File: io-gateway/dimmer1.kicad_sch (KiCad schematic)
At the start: 1 part, among them U1 LED5000

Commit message: update
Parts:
- added C22, C29, C33, C35: 100nF 50V, Capacitor_SMD:C_0201_0603Metric, symbol Device:C
- added C23, C36: 1µF 50V, Capacitor_SMD:C_1206_3216Metric, symbol Device:C
- added C24, C37: NM, Capacitor_SMD:C_1206_3216Metric, symbol Device:C
- added C25, C34: 22pF, Capacitor_SMD:C_0603_1608Metric, symbol Device:C
- added C26, C32: 470pF, Capacitor_SMD:C_0603_1608Metric, symbol Device:C
- added C27, C28, C30, C31: 10µF 50V, Capacitor_SMD:C_1210_3225Metric, symbol Device:C
- added D20, D23: D_Zener, Diode_SMD:D_SOD-123, symbol Device:D_Zener
- added D21, D22: D_Schottky, Diode_SMD:D_SMB, symbol Device:D_Schottky
- added L4, L5: 47µH 3.8A, Inductor_SMD:L_12x12mm_H8mm, symbol Device:L
- added R38, R41: 47k, Resistor_SMD:R_0603_1608Metric, symbol Device:R
- added R39, R40: 24k9, Resistor_SMD:R_0603_1608Metric, symbol Device:R
- added RS_DIM1, RS_DIM2: R, Resistor_SMD:R_1206_3216Metric, symbol Device:R
- added U2: LED5000, Package_SO:HSOP-8-1EP_3.9x4.9mm_P1.27mm_EP2.41x3.1mm, symbol Driver_LED:LED5000
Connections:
- net at U1.1 (BOOT): now also C22.1
- net PWM_DIM1: now reaches U1.2 (DIM)
- net INH_DIM1: now reaches U1.3 (INH)
- net at U1.4 (COMP): now also C25.1, R39.2
- net at U1.5 (FB): now also D20.2 (A), R38.2
- net GND: now reaches U1.6 (GND), U1.9 (GND)
- net GND: now also U1.7 (VIN), C23.2, C25.2, C26.2, C27.1, C27.2, C28.1, C28.2, C29.1, C29.2, C30.1, C30.2, C31.1, C31.2, C32.2, C33.1, C33.2, C34.2, C36.2, D21.2 (A), D22.2 (A), RS_DIM1.2, RS_DIM2.2, U2.6 (GND), U2.7 (VIN), U2.9 (GND)
- net at U1.8 (SW): now also C22.2, D21.1 (K), L4.2
- new net: C26.1, R39.1
- new net: C35.1, U2.1 (BOOT)
- new net: C34.1, R40.2, U2.4 (COMP)
- new net: D23.2 (A), R41.2, U2.5 (FB)
- new net: C35.2, D22.1 (K), L5.2, U2.8 (SW)
- new net: C32.1, R40.1
- new net DIM1_VLED+: C23.1, C24.1, D20.1 (K), L4.1
- new net DIM1_VLED-: C24.2, R38.1, RS_DIM1.1
- new net DIM2_VLED+: C36.1, C37.1, D23.1 (K), L5.1
- new net DIM2_VLED-: C37.2, R41.1, RS_DIM2.1
- new net INH_DIM2: U2.3 (INH)
- new net PWM_DIM2: U2.2 (DIM)
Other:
- moved on the sheet: U1

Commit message: layout for first dimmer
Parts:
- C22: footprint Capacitor_SMD:C_0201_0603Metric -> Capacitor_SMD:C_0603_1608Metric
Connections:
- net GND: no longer C27.1, C28.1, C29.1, C30.1, C31.1, C33.1, U1.7 (VIN), U2.7 (VIN)
- net DIM1_FB: now reaches D20.2 (A), R38.2, U1.5 (FB)
- net DIM1_SW: now reaches C22.2, D21.1 (K), L4.2, U1.8 (SW)
- net DIM1_VLED+ renamed DIM1_VLED_VCC
- net DIM1_VLED- renamed DIM1_VLED_GND
- net DIM2_VLED+ renamed DIM2_VLED_VCC
- net DIM2_VLED- renamed DIM2_VLED_GND
- new net VIN_DIM1: C27.1, C28.1, C29.1, C30.1, C31.1, C33.1, U1.7 (VIN), U2.7 (VIN)
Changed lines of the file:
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@@
 		)
 	)
-	(global_label "DIM1_VLED-"
-		(shape input)
-		(at 201.93 60.96 0)
-		(fields_autoplaced yes)
+	(label "DIM1_SW"
+		(at 114.3 46.99 0)
 		(effects
 			(font
 				(size 1.27 1.27)
 			)
+			(justify left bottom)
+		)
+	)
+	(label "DIM1_FB"
+		(at 114.3 49.53 0)
+		(effects
+			(font
+				(size 1.27 1.27)
+			)
+			(justify left bottom)
+		)
+	)
+	(global_label "DIM1_VLED_GND"
+		(shape input)
+		(at 201.93 60.96 0)
+		(fields_autoplaced yes)
+		(effects
+			(font
+				(size 1.27 1.27)
+			)
 			(justify left)
 		)
@@
 		)
 	)
-	(global_label "DIM1_VLED+"
+	(global_label "DIM1_VLED_VCC"
 		(shape input)
 		(at 201.93 46.99 0)
@@
 		)
 	)
-	(global_label "DIM2_VLED-"
+	(global_label "DIM2_VLED_GND"
 		(shape input)
 		(at 200.66 135.89 0)
@@
 		)
 	)
-	(global_label "VIN_DIM1"
+	(global_label "GND_DIM1"
 		(shape input)
 		(at 33.02 78.74 180)
@@
 		)
 		(property "Intersheetrefs" "${INTERSHEET_REFS}"
-			(at 21.5076 78.74 0)
+			(at 20.661 78.74 0)
 			(effects
 				(font
@@
 		)
 	)
-	(global_label "DIM2_VLED+"
+	(global_label "DIM2_VLED_VCC"
 		(shape input)
 		(at 200.66 121.92 0)
@@
 			)
 		)
-		(property "Footprint" "Capacitor_SMD:C_0201_0603Metric"
+		(property "Footprint" "Capacitor_SMD:C_0603_1608Metric"
 			(at 133.0452 46.99 0)
 			(effects

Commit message: upd
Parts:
- C29, C33, C35: footprint Capacitor_SMD:C_0201_0603Metric -> Capacitor_SMD:C_0603_1608Metric
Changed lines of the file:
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@@
 	)
 	(junction
+		(at 71.12 78.74)
+		(diameter 0)
+		(color 0 0 0 0)
+	)
+	(junction
 		(at 130.81 154.94)
 		(diameter 0)
@@
 	)
 	(junction
+		(at 38.1 78.74)
+		(diameter 0)
+		(color 0 0 0 0)
+	)
+	(junction
 		(at 96.52 154.94)
 		(diameter 0)
@@
 	(wire
 		(pts
+			(xy 71.12 78.74) (xy 71.12 80.01)
+		)
+		(stroke
+			(width 0)
+			(type default)
+		)
+	)
+	(wire
+		(pts
 			(xy 97.79 82.55) (xy 97.79 80.01)
 		)
@@
 	(wire
 		(pts
-			(xy 71.12 72.39) (xy 71.12 80.01)
+			(xy 71.12 72.39) (xy 71.12 78.74)
 		)
 		(stroke
@@
 	(wire
 		(pts
+			(xy 38.1 78.74) (xy 71.12 78.74)
+		)
+		(stroke
+			(width 0)
+			(type default)
+		)
+	)
+	(wire
+		(pts
 			(xy 31.75 121.92) (xy 86.36 121.92)
 		)
@@
 			)
 		)
-		(property "Footprint" "Capacitor_SMD:C_0201_0603Metric"
+		(property "Footprint" "Capacitor_SMD:C_0603_1608Metric"
 			(at 77.1652 107.95 0)
 			(effects
@@
 			)
 		)
-		(property "Footprint" "Capacitor_SMD:C_0201_0603Metric"
+		(property "Footprint" "Capacitor_SMD:C_0603_1608Metric"
 			(at 78.4352 33.02 0)
 			(effects
@@
 			)
 		)
-		(property "Footprint" "Capacitor_SMD:C_0201_0603Metric"
+		(property "Footprint" "Capacitor_SMD:C_0603_1608Metric"
 			(at 131.7752 121.92 0)
 			(effects

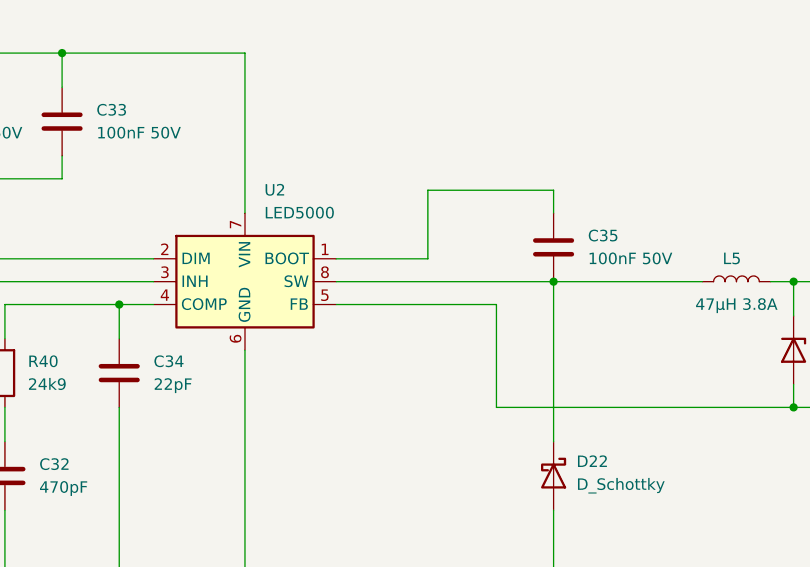
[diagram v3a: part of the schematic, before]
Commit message: add second dimmer
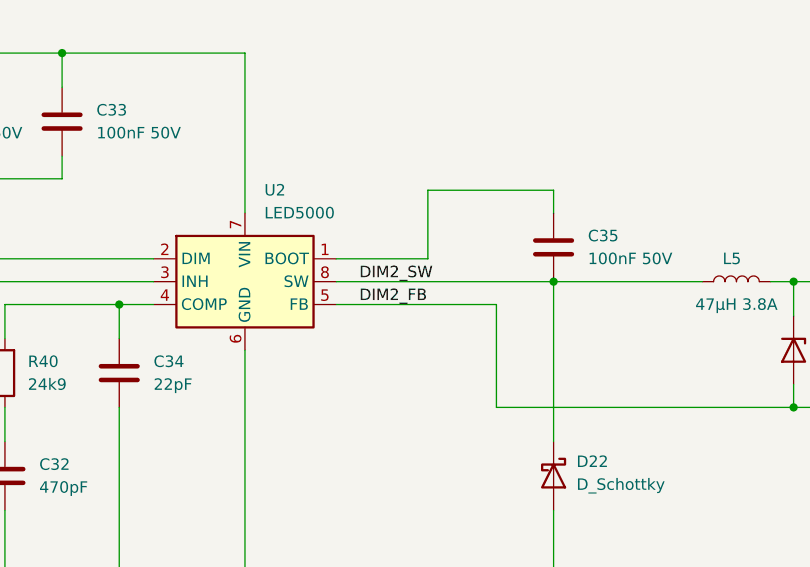
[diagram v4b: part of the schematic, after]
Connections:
- net DIM2_FB: now reaches D23.2 (A), R41.2, U2.5 (FB)
- net DIM2_SW: now reaches C35.2, D22.1 (K), L5.2, U2.8 (SW)
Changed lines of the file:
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@@
+		)
+	)
+	(label "DIM2_SW"
+		(at 109.22 121.92 0)
+		(effects
+			(font
+				(size 1.27 1.27)
+			)
+			(justify left bottom)
+		)
+	)
+	(label "DIM2_FB"
+		(at 109.22 124.46 0)
+		(effects
+			(font
+				(size 1.27 1.27)
+			)
+			(justify left bottom)
 		)
 	)

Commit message: temp
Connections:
- net DIM1_VLED_GND renamed DIM_VLED-_A
- net DIM1_VLED_VCC renamed DIM_VLED+_A
- net DIM2_VLED_GND renamed DIM_VLED-_B
- net DIM2_VLED_VCC renamed DIM_VLED+_B
- net INH_DIM1 renamed INH_DIMA
- net INH_DIM2 renamed INH_DIMB
- net PWM_DIM1 renamed PWM_DIMA
- net PWM_DIM2 renamed PWM_DIMB
- net VIN_DIM1 renamed VIN_DIM
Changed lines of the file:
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@@
 	(wire
 		(pts
-			(xy 31.75 119.38) (xy 86.36 119.38)
+			(xy 26.67 119.38) (xy 86.36 119.38)
 		)
 		(stroke
@@
 	(wire
 		(pts
-			(xy 195.58 46.99) (xy 201.93 46.99)
+			(xy 195.58 46.99) (xy 223.52 46.99)
 		)
 		(stroke
@@
 	(wire
 		(pts
-			(xy 195.58 60.96) (xy 201.93 60.96)
+			(xy 195.58 60.96) (xy 223.52 60.96)
 		)
 		(stroke
@@
 	(wire
 		(pts
-			(xy 194.31 135.89) (xy 200.66 135.89)
+			(xy 194.31 135.89) (xy 220.98 135.89)
 		)
 		(stroke
@@
 	(wire
 		(pts
-			(xy 33.02 46.99) (xy 87.63 46.99)
-		)
-		(stroke
-			(width 0)
-			(type default)
-		)
-	)
-	(wire
-		(pts
 			(xy 83.82 60.96) (xy 83.82 80.01)
 		)
@@
 	(wire
 		(pts
+			(xy 21.59 21.59) (xy 43.18 21.59)
+		)
+		(stroke
+			(width 0)
+			(type default)
+		)
+	)
+	(wire
+		(pts
 			(xy 191.77 46.99) (xy 195.58 46.99)
 		)
@@
 	(wire
 		(pts
+			(xy 24.13 44.45) (xy 87.63 44.45)
+		)
+		(stroke
+			(width 0)
+			(type default)
+		)
+	)
+	(wire
+		(pts
 			(xy 96.52 157.48) (xy 96.52 154.94)
 		)
@@
 	(wire
 		(pts
-			(xy 33.02 44.45) (xy 87.63 44.45)
-		)
-		(stroke
-			(width 0)
-			(type default)
-		)
-	)
-	(wire
-		(pts
 			(xy 177.8 80.01) (xy 191.77 80.01)
 		)
@@
 	(wire
 		(pts
-			(xy 43.18 21.59) (xy 31.75 21.59)
-		)
-		(stroke
-			(width 0)
-			(type default)
-		)
-	)
-	(wire
-		(pts
 			(xy 132.08 36.83) (xy 132.08 39.37)
 		)
@@
 	(wire
 		(pts
-			(xy 194.31 121.92) (xy 200.66 121.92)
+			(xy 194.31 121.92) (xy 220.98 121.92)
 		)
 		(stroke
@@
 	(wire
 		(pts
+			(xy 24.13 46.99) (xy 87.63 46.99)
+		)
+		(stroke
+			(width 0)
+			(type default)
+		)
+	)
+	(wire
+		(pts
 			(xy 41.91 107.95) (xy 41.91 110.49)
 		)
@@
 	(wire
 		(pts
-			(xy 33.02 78.74) (xy 38.1 78.74)
-		)
-		(stroke
-			(width 0)
-			(type default)
-		)
-	)
-	(wire
-		(pts
 			(xy 96.52 114.3) (xy 96.52 96.52)
 		)
@@
 	(wire
 		(pts
-			(xy 31.75 121.92) (xy 86.36 121.92)
+			(xy 26.67 121.92) (xy 86.36 121.92)
 		)
 		(stroke
@@
 		(pts
 			(xy 96.52 154.94) (xy 130.81 154.94)
+		)
+		(stroke
+			(width 0)
+			(type default)
+		)
+	)
+	(wire
+		(pts
+			(xy 22.86 78.74) (xy 38.1 78.74)
 		)
 		(stroke
@@
 		)
 	)
+	(label "VIN_DIM"
+		(at 30.48 96.52 0)
+		(effects
+			(font
+				(size 1.27 1.27)
+			)
+			(justify left bottom)
+		)
+	)
 	(label "DIM2_SW"
 		(at 109.22 121.92 0)
@@
 		)
 	)
-	(global_label "DIM1_VLED_GND"
+	(hierarchical_label "INH_DIMB"
 		(shape input)
-		(at 201.93 60.96 0)
-		(fields_autoplaced yes)
+		(at 26.67 121.92 180)
+		(effects
+			(font
+				(size 1.27 1.27)
+			)
+			(justify right)
+		)
+	)
+	(hierarchical_label "DIM_VLED+_A"
+		(shape output)
+		(at 223.52 46.99 0)
 		(effects
 			(font
@@
 			(justify left)
 		)
-		(property "Intersheetrefs" "${INTERSHEET_REFS}"
-			(at 216.5266 60.96 0)
-			(effects
-				(font
-					(size 1.27 1.27)
-				)
-				(justify left)
-				(hide yes)
-			)
-		)
-	)
-	(global_label "VIN_DIM1"
+	)
+	(hierarchical_label "DIM_VLED-_A"
+		(shape output)
+		(at 223.52 60.96 0)
+		(effects
+			(font
+				(size 1.27 1.27)
+			)
+			(justify left)
+		)
+	)
+	(hierarchical_label "VIN_DIM"
 		(shape input)
-		(at 31.75 21.59 180)
-		(fields_autoplaced yes)
+		(at 21.59 21.59 180)
 		(effects
 			(font
@@
 			(justify right)
 		)
-		(property "Intersheetrefs" "${INTERSHEET_REFS}"
-			(at 20.2376 21.59 0)
-			(effects
-				(font
-					(size 1.27 1.27)
-				)
-				(justify right)
-				(hide yes)
-			)
-		)
-	)
-	(global_label "DIM1_VLED_VCC"
+	)
+	(hierarchical_label "INH_DIMA"
 		(shape input)
-		(at 201.93 46.99 0)
-		(fields_autoplaced yes)
+		(at 24.13 46.99 180)
+		(effects
+			(font
+				(size 1.27 1.27)
+			)
+			(justify right)
+		)
+	)
+	(hierarchical_label "PWM_DIMB"
+		(shape input)
+		(at 26.67 119.38 180)
+		(effects
+			(font
+				(size 1.27 1.27)
+			)
+			(justify right)
+		)
+	)
+	(hierarchical_label "DIM_VLED+_B"
+		(shape output)
+		(at 220.98 121.92 0)
 		(effects
 			(font
@@
 			(justify left)
 		)
-		(property "Intersheetrefs" "${INTERSHEET_REFS}"
-			(at 216.5266 46.99 0)
-			(effects
-				(font
-					(size 1.27 1.27)
-				)
-				(justify left)
-				(hide yes)
-			)
-		)
-	)
-	(global_label "PWM_DIM1"
+	)
+	(hierarchical_label "PWM_DIMA"
 		(shape input)
-		(at 33.02 44.45 180)
-		(fields_autoplaced yes)
+		(at 24.13 44.45 180)
 		(effects
 			(font
@@
 			(justify right)
 		)
-		(property "Intersheetrefs" "${INTERSHEET_REFS}"
-			(at 20.3587 44.45 0)
-			(effects
-				(font
-					(size 1.27 1.27)
-				)
-				(justify right)
-				(hide yes)
-			)
-		)
-	)
-	(global_label "VIN_DIM1"
+	)
+	(hierarchical_label "GND_DIM"
 		(shape input)
-		(at 30.48 96.52 180)
-		(fields_autoplaced yes)
+		(at 22.86 78.74 180)
 		(effects
 			(font
@@
 			(justify right)
 		)
-		(property "Intersheetrefs" "${INTERSHEET_REFS}"
-			(at 18.9676 96.52 0)
-			(effects
-				(font
-					(size 1.27 1.27)
-				)
-				(justify right)
-				(hide yes)
-			)
-		)
-	)
-	(global_label "DIM2_VLED_GND"
-		(shape input)
-		(at 200.66 135.89 0)
-		(fields_autoplaced yes)
+	)
+	(hierarchical_label "DIM_VLED-_B"
+		(shape output)
+		(at 220.98 135.89 0)
 		(effects
 			(font
@@
 			(justify left)
 		)
-		(property "Intersheetrefs" "${INTERSHEET_REFS}"
-			(at 215.2566 135.89 0)
-			(effects
-				(font
-					(size 1.27 1.27)
-				)
-				(justify left)
-				(hide yes)
-			)
-		)
-	)
-	(global_label "GND_DIM1"
-		(shape input)
-		(at 33.02 78.74 180)
-		(fields_autoplaced yes)
-		(effects
-			(font
-				(size 1.27 1.27)
-			)
-			(justify right)
-		)
-		(property "Intersheetrefs" "${INTERSHEET_REFS}"
-			(at 20.661 78.74 0)
-			(effects
-				(font
-					(size 1.27 1.27)
-				)
-				(justify right)
-				(hide yes)
-			)
-		)
-	)
-	(global_label "PWM_DIM2"
-		(shape input)
-		(at 31.75 119.38 180)
-		(fields_autoplaced yes)
-		(effects
-			(font
-				(size 1.27 1.27)
-			)
-			(justify right)
-		)
-		(property "Intersheetrefs" "${INTERSHEET_REFS}"
-			(at 19.0887 119.38 0)
-			(effects
-				(font
-					(size 1.27 1.27)
-				)
-				(justify right)
-				(hide yes)
-			)
-		)
-	)
-	(global_label "INH_DIM2"
-		(shape input)
-		(at 31.75 121.92 180)
-		(fields_autoplaced yes)
-		(effects
-			(font
-				(size 1.27 1.27)
-			)
-			(justify right)
-		)
-		(property "Intersheetrefs" "${INTERSHEET_REFS}"
-			(at 19.9957 121.92 0)
-			(effects
-				(font
-					(size 1.27 1.27)
-				)
-				(justify right)
-				(hide yes)
-			)
-		)
-	)
-	(global_label "INH_DIM1"
-		(shape input)
-		(at 33.02 46.99 180)
-		(fields_autoplaced yes)
-		(effects
-			(font
-				(size 1.27 1.27)
-			)
-			(justify right)
-		)
-		(property "Intersheetrefs" "${INTERSHEET_REFS}"
-			(at 21.2657 46.99 0)
-			(effects
-				(font
-					(size 1.27 1.27)
-				)
-				(justify right)
-				(hide yes)
-			)
-		)
-	)
-	(global_label "DIM2_VLED_VCC"
-		(shape input)
-		(at 200.66 121.92 0)
-		(fields_autoplaced yes)
-		(effects
-			(font
-				(size 1.27 1.27)
-			)
-			(justify left)
-		)
-		(property "Intersheetrefs" "${INTERSHEET_REFS}"
-			(at 215.2566 121.92 0)
-			(effects
-				(font
-					(size 1.27 1.27)
-				)
-				(justify left)
-				(hide yes)
-			)
-		)
-	)
+	)

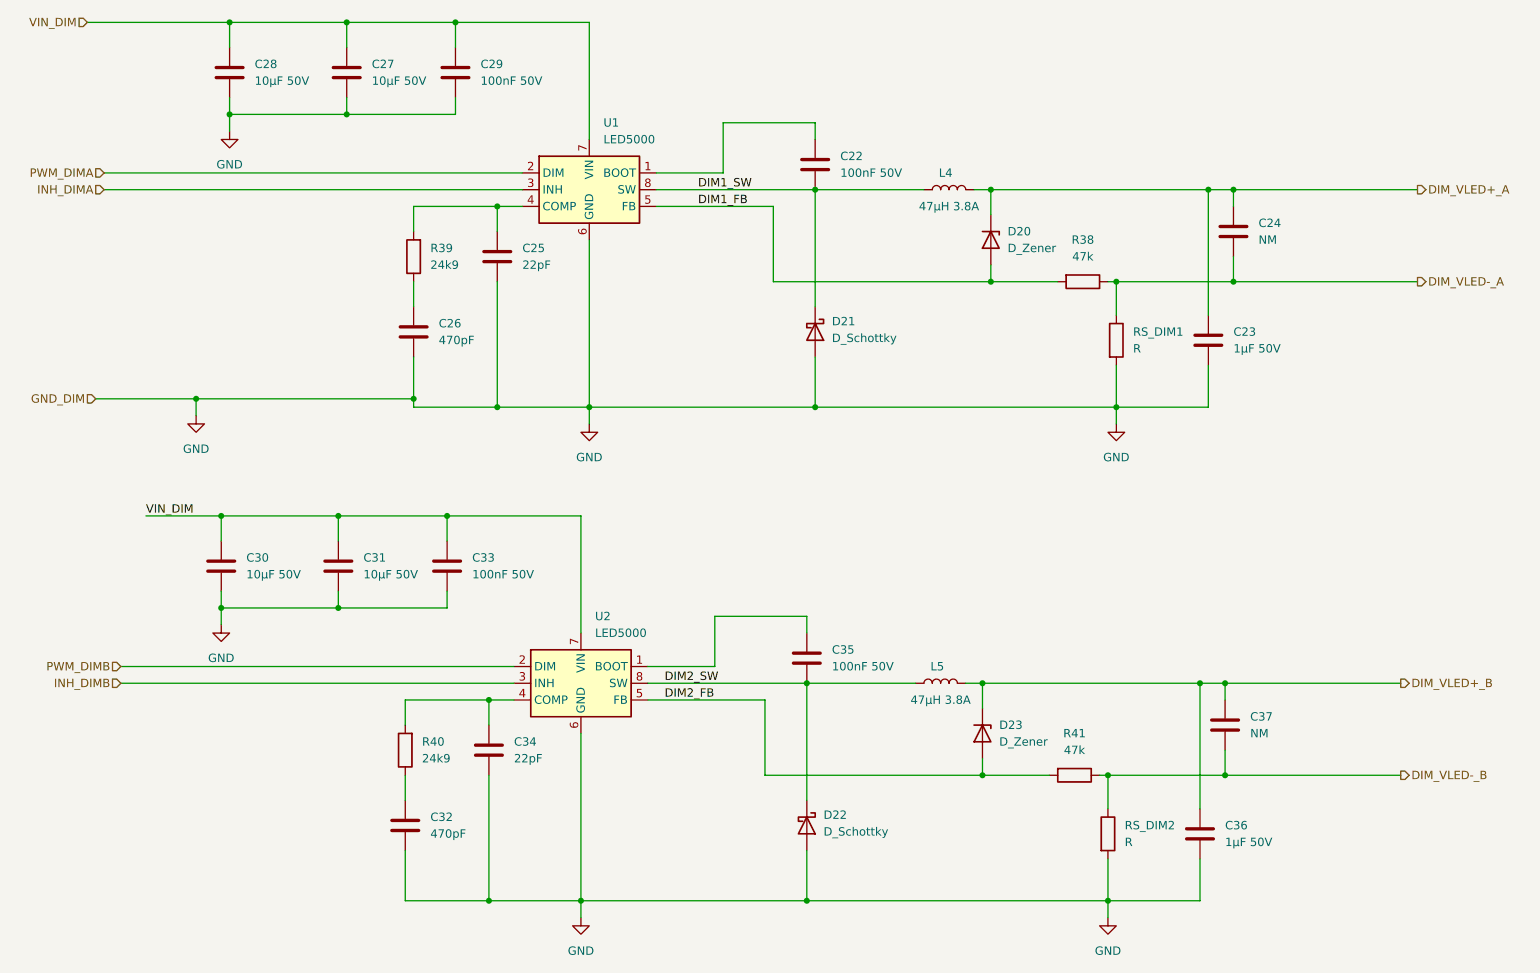
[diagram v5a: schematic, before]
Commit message: reannotate dimmers and relays
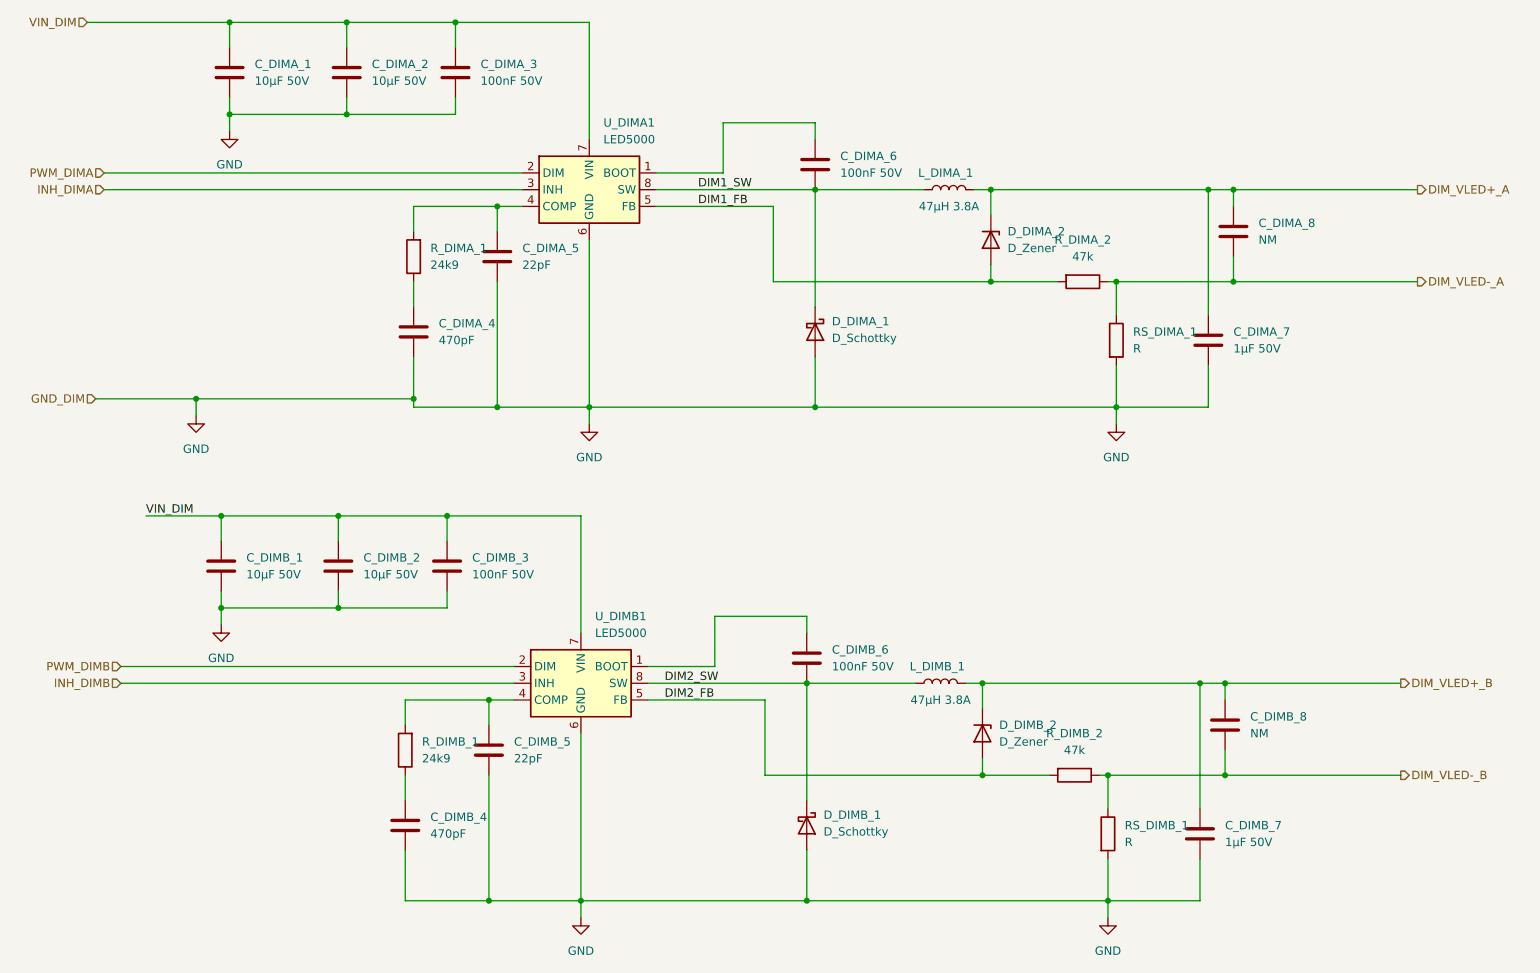
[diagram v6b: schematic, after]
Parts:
- renumbered C28 to C_DIMA_1, C27 to C_DIMA_2, C29 to C_DIMA_3, C26 to C_DIMA_4, C25 to C_DIMA_5, C22 to C_DIMA_6, C23 to C_DIMA_7, C24 to C_DIMA_8, C30 to C_DIMB_1, C31 to C_DIMB_2, C33 to C_DIMB_3, C32 to C_DIMB_4, C34 to C_DIMB_5, C35 to C_DIMB_6, C36 to C_DIMB_7, C37 to C_DIMB_8, D21 to D_DIMA_1, D20 to D_DIMA_2, D22 to D_DIMB_1, D23 to D_DIMB_2, L4 to L_DIMA_1, L5 to L_DIMB_1, RS_DIM1 to RS_DIMA_1, RS_DIM2 to RS_DIMB_1, R39 to R_DIMA_1, R38 to R_DIMA_2, R40 to R_DIMB_1, R41 to R_DIMB_2, U1 to U_DIMA1, U2 to U_DIMB1
